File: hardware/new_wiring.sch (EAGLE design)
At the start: 44 parts, among them SW1 ROTARTY_ENCODER, T1 100 C, T2 140 C, T3 160 C

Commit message: updated wiring
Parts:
- removed SW1: ROTARTY_ENCODER, SparkFun-Electromechanical:ROTARTY_ENCODER
- added R11, R12, R13, R14: 10k, rcl:R-EU_0613/5V
- added S5: MAINS ON/OFF, switch-misc:PVA1
- added SSR3: SPARE, relay:S101T01
- added T6, T7: (no value), usr_gerneral:N/P-MOS-DMG1029SV
- R10: value 470 ??? -> 10k
- U$1, U$2: value LM35 TEMP-SENSOR -> LMT87 TEMP-SENSOR
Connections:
- new net CTRL_SPARE_BH_HEATER: R11.1, T6-N.G
- new net N$13: S11.P, S21.P, S31.P, S51.S, SSR1.DS2, SSR2.DS2
- new net N$14: S12.P, S22.P, S32.P, S52.S, T3.1, TP2.TP
- new net N$28: SSR3.K, T6-N.D
- net +12V: now also SSR3.A
- net +3V3: no longer LED1.A
- net +5V: now also LED1.A
- net GND: now also R10.1, R11.2, T6-N.S, T7-N.S
- net LED_ON_OFF: now also LED1.C, T7-N.D; no longer R10.1
- net N$12: now also T7-N.G; no longer LED1.C
- net VEE: now also S51.P; no longer S11.P, S21.P, S31.P, SSR1.DS2, SSR2.DS2
- net VPP: now also S52.P; no longer S12.P, S22.P, S32.P, T3.1, TP2.TP
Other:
- note added: "5 Kabel zu uC 6 Kabel Schalter (Schraubklemmen)"
- note added: "5V LED"
- note added: "?"
- note added: "LED: 0,1mA @ 5V"
- note added: "black"
- note added: "digital out"
- note added: "incorrect package for MID400"
- note added: "needed?"
- note added: "red"
- note removed: "Ausschaltlogik???"
- note removed: "drei kleine Platinen jeweils hinter switch 2 Kabel rein 3 Kabel raus"
- moved on the sheet: HEATER, IC1, LED1, R1, R10, R2, R9, S4, SG1, SSR1, SSR2, T1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

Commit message: adopted final MID400 values ; moved valve to support SSR ; added analog-in C
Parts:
- added C7, C8, C9: 1u, rcl:C-EU025-024X044
- C4, C5, C6: value 10n -> 3n3
- SSR3: value SPARE -> VALVE
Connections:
- net CTRL_SPARE_BH_HEATER renamed CTRL_VALVE
- new net N$29: SSR3.DS1
- net GND: now also C7.2, C8.2, C9.2
- net N$13: now also SSR3.DS2
- net SENS_BOILER: now also C7.1
- net SENS_BREWHEAD: now also C8.1
- net SENS_TC_BOILER: now also C9.1
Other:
- note added: "5 cables to uC 6 cables to crimp connectors"
- note added: "USB-cable"
- note added: "ground"
- note added: "it seems that LED has internal resistor"
- note removed: "5 Kabel zu uC 6 Kabel Schalter (Schraubklemmen)"
- note removed: "?"
- moved on the sheet: HEATER, S5, T1, T2, T3

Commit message: hardware pin definitions
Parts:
- added C10, C11, C12: 100n, rcl:C-EU025-024X044
- added R17: 1k8 72mW, rcl:R-EU_0613/5V
- C7, C8, C9: value 1u -> 100n
- SSR1_HEATER: value HEATER -> SSR-40 DA
- SSR2_PUMP: value PUMP -> SSR-40 DA
- SSR3_VALVE: value VALVE -> CPC1976Y
- U$3: value Thermocouple Board -> LMT87 TEMP-SENSOR
- renumbered SSR1 to SSR1_HEATER, SSR2 to SSR2_PUMP, SSR3 to SSR3_VALVE
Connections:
- net SENS_TC_BOILER renamed SENS_BOILER_TOP
- new net ENC_BTN: C10.1
- new net ENC_CLK: C12.1
- new net ENC_DT: C11.1
- new net N$30: R17.2, SSR3_VALVE.K
- net +3V3: now also R9.2; no longer S4.S
- net BUTTON_ON_OFF: now also R9.1; no longer R9.2
- net GND: now also C10.2, C11.2, C12.2, S4.S; no longer R9.1
- net N$28: now also R17.1; no longer SSR3_VALVE.K
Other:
- note added: "16"
- note added: "17"
- note added: "21"
- note added: "22"
- note added: "23"
- note added: "25"
- note added: "26"
- note added: "27"
- note added: "33"
- note added: "3v3: 1: switch monitor board 2: display 3: rotary encoder 4: temp sensor 1 5: temp sensor 2 6: temp sensor 3"
- note added: "4"
- note added: "5v: 1: power LED 2: 12v step-up"
- note added: "?"
- note added: "A0"
- note added: "A3"
- note added: "A6"
- note added: "GND: 1: switch monitor board 2: display + shield 3: rotary encoder 4: temp sensor 1 + shield 5: temp sensor 2 + shield 6: temp sensor 3 + shield 7: 12v step-up 8: power switch"
- note added: "I2C pull-ups are integrated in display"
- note added: "ground y/g"
- note added: "maybe supply valve SSR with less V"
- note added: "rd: 3v3 bk: GND yl: signal 1 gn: signal 2 wt: signal 3"
- note removed: "ground"
- moved on the sheet: C8, C9, LED1, R10, R9, SG1, T7-N

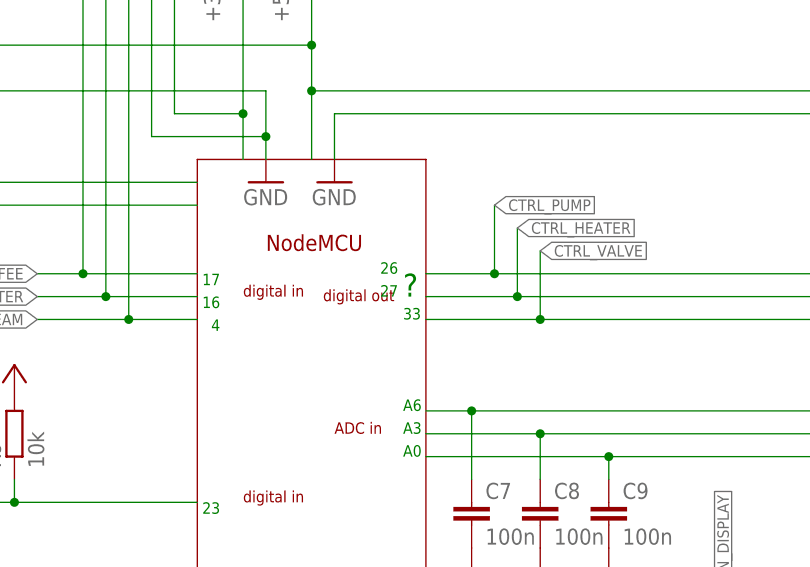
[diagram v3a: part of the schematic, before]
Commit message: found out wiring for heater
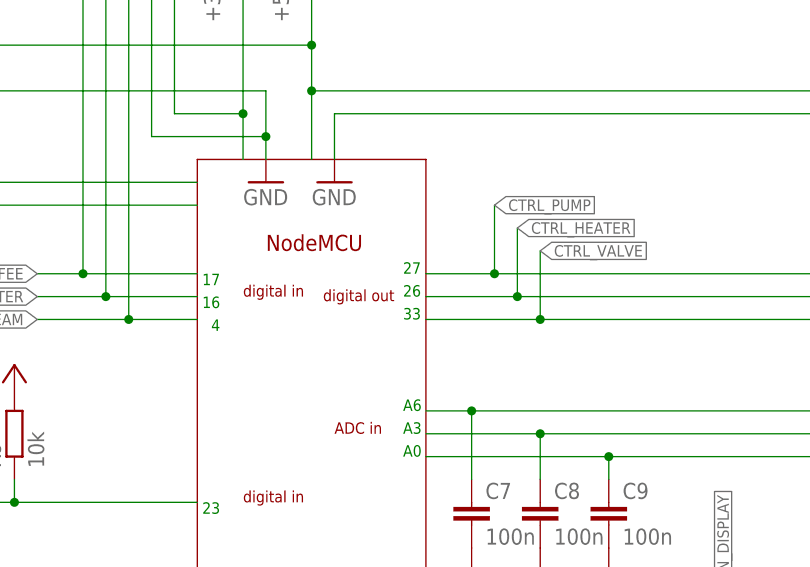
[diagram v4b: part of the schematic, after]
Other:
- note removed: "?"
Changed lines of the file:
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@@
 <text x="355.6" y="-5.08" size="1.778" layer="94">I2C pull-ups are integrated in display</text>
 <text x="248.92" y="35.56" size="1.27" layer="91">33</text>
-<text x="246.38" y="40.64" size="1.27" layer="91">26</text>
-<text x="246.38" y="38.1" size="1.27" layer="91">27</text>
+<text x="248.92" y="38.1" size="1.27" layer="91">26</text>
+<text x="248.92" y="40.64" size="1.27" layer="91">27</text>
 <text x="228.6" y="0" size="1.27" layer="91" rot="R180">25</text>
 <text x="81.28" y="27.94" size="1.778" layer="94" rot="MR180">3v3:
@@
 valve SSR with less V</text>
 <text x="228.6" y="15.24" size="1.27" layer="91" rot="R180">23</text>
-<text x="248.92" y="38.1" size="2.54" layer="91">?</text>
 <text x="228.6" y="40.64" size="1.27" layer="91" rot="R180">17</text>
 <text x="228.6" y="38.1" size="1.27" layer="91" rot="R180">16</text>

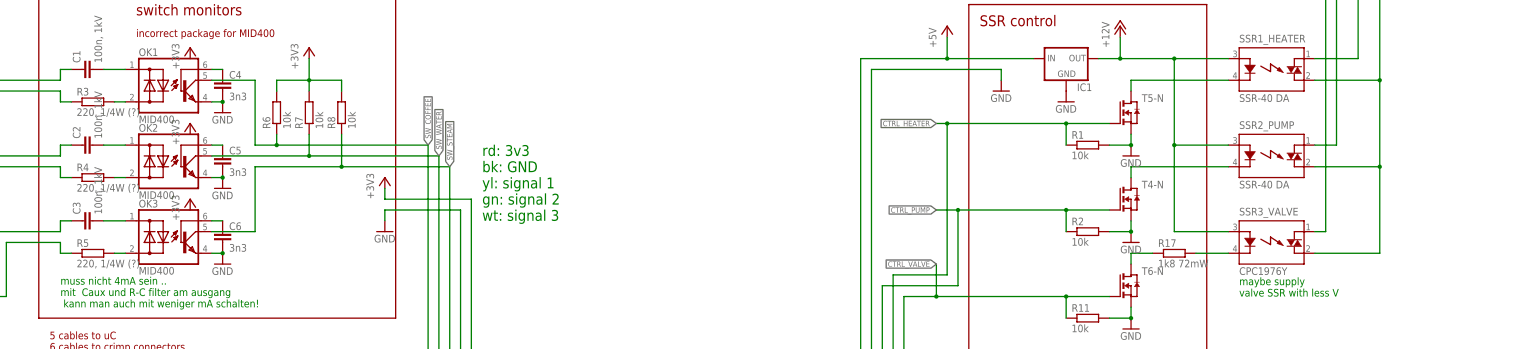
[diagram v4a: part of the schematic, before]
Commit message: added RC-snubber to SSR outputs (valve, pump)
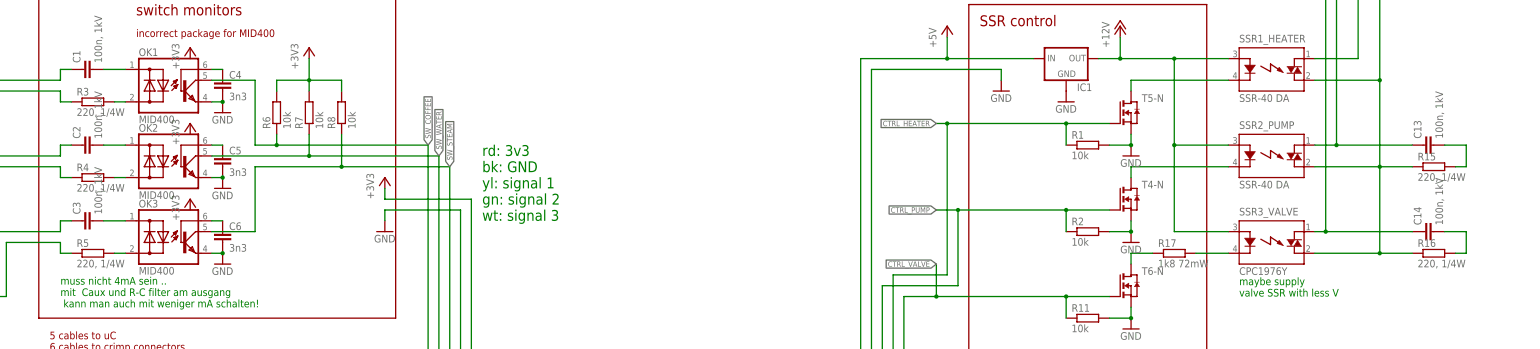
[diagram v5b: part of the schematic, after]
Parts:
- added C13, C14: 100n, 1kV, rcl:C-EU025-024X044
- added R15, R16: 220, 1/4W, rcl:R-EU_0613/5V
- R3, R4, R5: value 220, 1/4W (?) -> 220, 1/4W
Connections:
- new net N$31: C13.2, R15.2
- new net N$32: C14.2, R16.2
- net N$1: now also C13.1
- net N$13: now also R15.1, R16.1
- net N$29: now also C14.1
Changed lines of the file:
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@@
 <part name="GND8" library="supply1" deviceset="GND" device=""/>
 <part name="GND9" library="supply1" deviceset="GND" device=""/>
-<part name="R3" library="rcl" deviceset="R-EU_" device="0613/5V" value="220, 1/4W (?)"/>
+<part name="R3" library="rcl" deviceset="R-EU_" device="0613/5V" value="220, 1/4W"/>
 <part name="C1" library="rcl" deviceset="C-EU" device="025-024X044" value="100n, 1kV"/>
 <part name="C2" library="rcl" deviceset="C-EU" device="025-024X044" value="100n, 1kV"/>
 <part name="C3" library="rcl" deviceset="C-EU" device="025-024X044" value="100n, 1kV"/>
-<part name="R4" library="rcl" deviceset="R-EU_" device="0613/5V" value="220, 1/4W (?)"/>
-<part name="R5" library="rcl" deviceset="R-EU_" device="0613/5V" value="220, 1/4W (?)"/>
+<part name="R4" library="rcl" deviceset="R-EU_" device="0613/5V" value="220, 1/4W"/>
+<part name="R5" library="rcl" deviceset="R-EU_" device="0613/5V" value="220, 1/4W"/>
 <part name="C4" library="rcl" deviceset="C-EU" device="025-024X044" value="3n3"/>
 <part name="C5" library="rcl" deviceset="C-EU" device="025-024X044" value="3n3"/>
@@
 <part name="R17" library="rcl" deviceset="R-EU_" device="0613/5V" value="1k8 72mW"/>
 <part name="+3V1" library="supply1" deviceset="+3V3" device=""/>
+<part name="R15" library="rcl" deviceset="R-EU_" device="0613/5V" value="220, 1/4W"/>
+<part name="C13" library="rcl" deviceset="C-EU" device="025-024X044" value="100n, 1kV"/>
+<part name="R16" library="rcl" deviceset="R-EU_" device="0613/5V" value="220, 1/4W"/>
+<part name="C14" library="rcl" deviceset="C-EU" device="025-024X044" value="100n, 1kV"/>
 </parts>
 <sheets>
@@
 <instance part="R17" gate="G$1" x="388.62" y="111.76"/>
 <instance part="+3V1" gate="G$1" x="205.74" y="30.48"/>
+<instance part="R15" gate="G$1" x="449.58" y="132.08"/>
+<instance part="C13" gate="G$1" x="447.04" y="137.16" rot="R90"/>
+<instance part="R16" gate="G$1" x="449.58" y="111.76"/>
+<instance part="C14" gate="G$1" x="447.04" y="116.84" rot="R90"/>
 </instances>
 <busses>
@@
 <pinref part="SSR2_PUMP" gate="1" pin="DS1"/>
 <wire x1="426.72" y1="137.16" x2="421.64" y2="137.16" width="0.1524" layer="91"/>
+<pinref part="C13" gate="G$1" pin="1"/>
+<wire x1="426.72" y1="137.16" x2="444.5" y2="137.16" width="0.1524" layer="91"/>
+<junction x="426.72" y="137.16"/>
 </segment>
 </net>
@@
 <pinref part="SSR3_VALVE" gate="1" pin="DS2"/>
 <wire x1="436.88" y1="111.76" x2="421.64" y2="111.76" width="0.1524" layer="91"/>
+<pinref part="R15" gate="G$1" pin="1"/>
+<wire x1="436.88" y1="132.08" x2="444.5" y2="132.08" width="0.1524" layer="91"/>
+<pinref part="R16" gate="G$1" pin="1"/>
+<wire x1="436.88" y1="111.76" x2="444.5" y2="111.76" width="0.1524" layer="91"/>
+<junction x="436.88" y="111.76"/>
 </segment>
 </net>
@@
 <pinref part="SSR3_VALVE" gate="1" pin="DS1"/>
 <wire x1="424.18" y1="116.84" x2="421.64" y2="116.84" width="0.1524" layer="91"/>
+<pinref part="C14" gate="G$1" pin="1"/>
+<wire x1="424.18" y1="116.84" x2="444.5" y2="116.84" width="0.1524" layer="91"/>
+<junction x="424.18" y="116.84"/>
 </segment>
 </net>
@@
 </segment>
 </net>
+<net name="N$31" class="0">
+<segment>
+<pinref part="C13" gate="G$1" pin="2"/>
+<wire x1="452.12" y1="137.16" x2="457.2" y2="137.16" width="0.1524" layer="91"/>
+<wire x1="457.2" y1="137.16" x2="457.2" y2="132.08" width="0.1524" layer="91"/>
+<pinref part="R15" gate="G$1" pin="2"/>
+<wire x1="457.2" y1="132.08" x2="454.66" y2="132.08" width="0.1524" layer="91"/>
+</segment>
+</net>
+<net name="N$32" class="0">
+<segment>
+<pinref part="C14" gate="G$1" pin="2"/>
+<wire x1="452.12" y1="116.84" x2="457.2" y2="116.84" width="0.1524" layer="91"/>
+<wire x1="457.2" y1="116.84" x2="457.2" y2="111.76" width="0.1524" layer="91"/>
+<pinref part="R16" gate="G$1" pin="2"/>
+<wire x1="457.2" y1="111.76" x2="454.66" y2="111.76" width="0.1524" layer="91"/>
+</segment>
+</net>
